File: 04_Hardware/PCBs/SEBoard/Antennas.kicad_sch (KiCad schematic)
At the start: 23 parts, among them J18 636101112001, J19 636101112001, J20 636101112001, J21 636101112001, U1 SC200EEMNA-E53-UGNDA

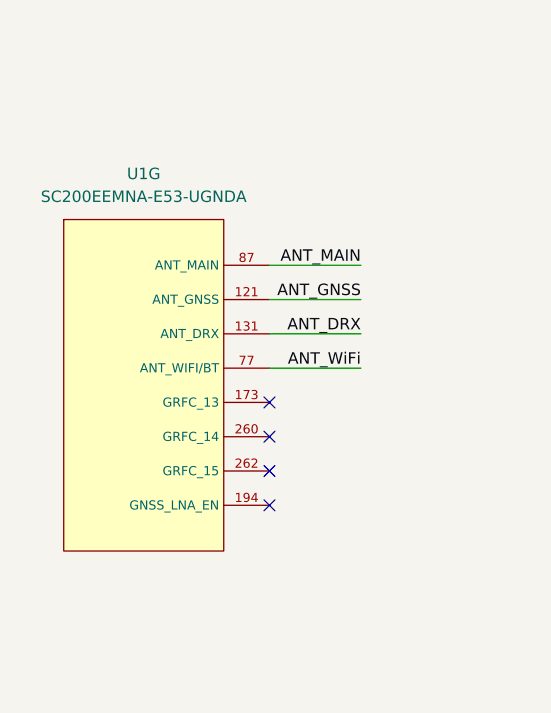
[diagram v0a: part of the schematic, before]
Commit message: feat(schematic): add SE250B4 symbol to schematic (unchecked)
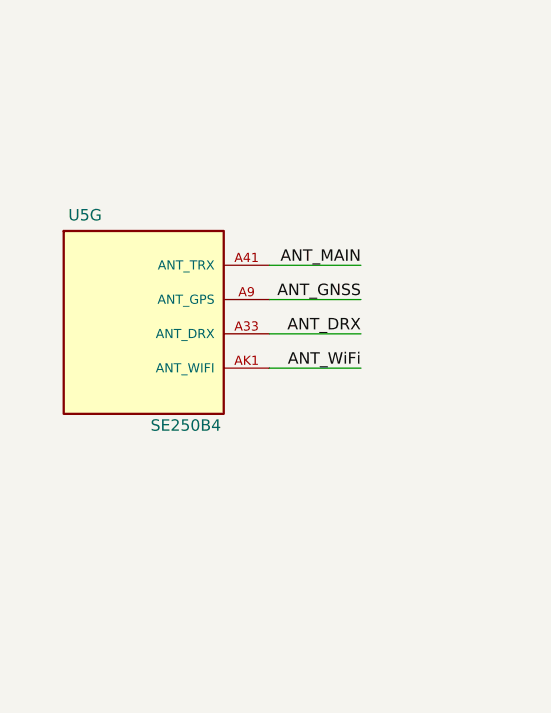
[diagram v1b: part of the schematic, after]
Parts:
- removed U1: SC200EEMNA-E53-UGNDA, SEBoard:SC200E_SC206E, symbol SEBoard:SC200E
- added U5: SE250B4, 000MCLib:XCVR_SE250B4-NA, symbol 000MCLib:SE250B4
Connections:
- net ANT_DRX: now also U5.A33 (ANT_DRX)
- net ANT_GNSS: now also U5.A9 (ANT_GPS)
- net ANT_MAIN: now also U5.A41 (ANT_TRX)
- net ANT_WiFi: now also U5.AK1 (ANT_WIFI)
- no-connect marks 4 -> 0

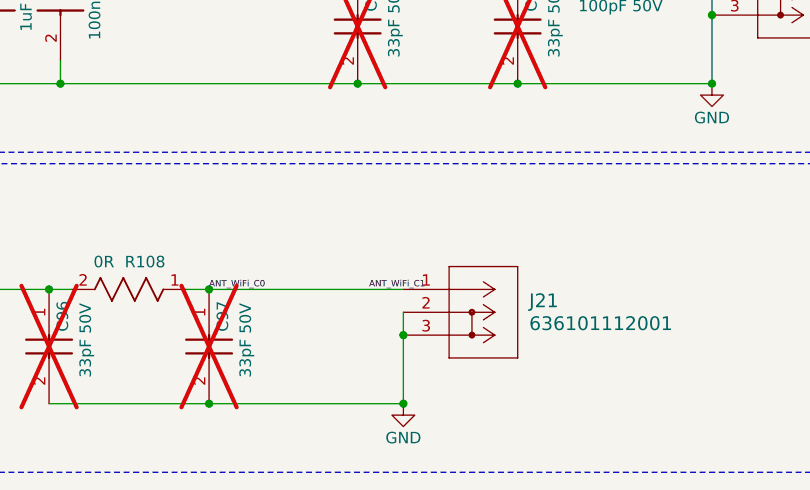
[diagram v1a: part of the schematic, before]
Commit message: feat: Updated schematic layout and moved new components to Layout
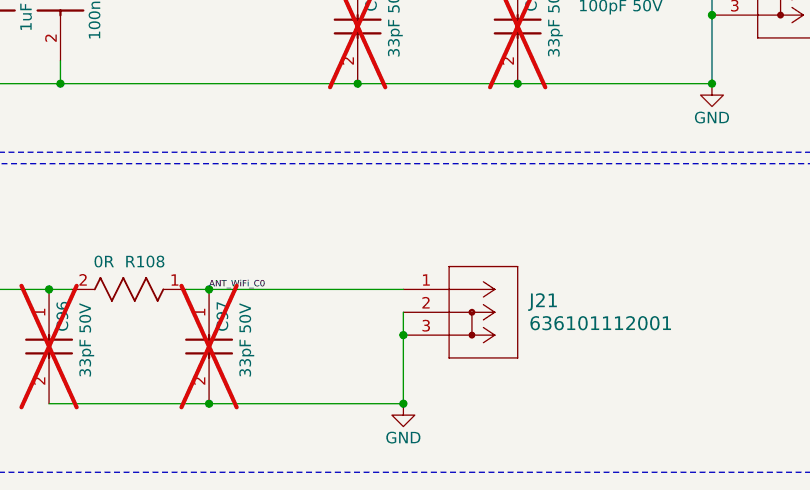
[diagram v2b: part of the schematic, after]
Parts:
- C51: footprint SEBoard:CAPC1005X55N -> 000MCLib:CAPC1005X55N; symbol SEBoard:GRM1555C1H101JA01J -> 000MCLib:GRM1555C1H101JA01J
- C53: footprint SEBoard:CAPC1005X55N -> 000MCLib:CAPC1005X55N; symbol SEBoard:GRM155R61H105KE05D -> 000MCLib:GRM155R61H105KE05D
- C55: footprint SEBoard:CAPC1005X55N -> 000MCLib:CAPC1005X55N; symbol SEBoard:GRM155R71A104KA01D -> 000MCLib:GRM155R71A104KA01D
- C90, C91, C92, C93, C94, C95, C96, C97: footprint SEBoard:CAPC1005X55N -> 000MCLib:CAPC1005X55N; symbol SEBoard:GRM1555C1H330JA01D -> 000MCLib:GRM1555C1H330JA01D
- J18, J19, J20, J21: footprint SEBoard:COAX2_636101112001_WRE -> 000MCLib:COAX2_636101112001_WRE; symbol SEBoard:636101112001 -> 000MCLib:636101112001
- L2: footprint SEBoard:INDC1005X60N -> 000MCLib:INDC1005X60N; symbol SEBoard:744784156A -> 000MCLib:744784156A
- R105, R106, R107, R108: footprint SEBoard:RC0402N_YAG -> 000MCLib:RC0402N_YAG; symbol SEBoard:RC0402JR-070RL -> 000MCLib:RC0402JR-070RL
- R16: footprint SEBoard:RC0402N_YAG -> 000MCLib:RC0402N_YAG; symbol SEBoard:RC0402JR-0710RL -> 000MCLib:RC0402JR-0710RL
- R69: footprint SEBoard:RESC2012X50N -> 000MCLib:RESC2012X50N; symbol SEBoard:CRCW08050000Z0EA -> 000MCLib:CRCW08050000Z0EA
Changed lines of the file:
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@@
 		)
 	)
-	(label "ANT_WiFi_C1"
-		(at 194.31 128.27 0)
-		(effects
-			(font
-				(size 0.7 0.7)
-			)
-			(justify left bottom)
-		)
-	)
 	(label "ANT_MAIN"
 		(at 72.39 82.55 180)
@@
 	)
 	(symbol
-		(lib_id "SEBoard:GRM155R61H105KE05D")
+		(lib_id "000MCLib:GRM155R61H105KE05D")
 		(at 152.4 96.52 270)
 		(unit 1)
@@
 			)
 		)
-		(property "Footprint" "SEBoard:CAPC1005X55N"
+		(property "Footprint" "000MCLib:CAPC1005X55N"
 			(at 56.21 105.41 0)
 			(effects
@@
 	)
 	(symbol
-		(lib_id "SEBoard:RC0402JR-0710RL")
+		(lib_id "000MCLib:RC0402JR-0710RL")
 		(at 204.47 83.82 0)
 		(unit 1)
@@
 			)
 		)
-		(property "Footprint" "SEBoard:RC0402N_YAG"
+		(property "Footprint" "000MCLib:RC0402N_YAG"
 			(at 198.12 83.82 0)
 			(effects
@@
 	)
 	(symbol
-		(lib_id "SEBoard:744784156A")
+		(lib_id "000MCLib:744784156A")
 		(at 218.44 83.82 0)
 		(unit 1)
@@
 			)
 		)
-		(property "Footprint" "SEBoard:INDC1005X60N"
+		(property "Footprint" "000MCLib:INDC1005X60N"
 			(at 234.95 180.01 0)
 			(effects
@@
 	)
 	(symbol
-		(lib_id "SEBoard:RC0402JR-070RL")
+		(lib_id "000MCLib:RC0402JR-070RL")
 		(at 167.64 128.27 0)
 		(unit 1)
@@
 			)
 		)
-		(property "Footprint" "SEBoard:RC0402N_YAG"
+		(property "Footprint" "000MCLib:RC0402N_YAG"
 			(at 161.29 128.27 0)
 			(effects
@@
 	)
 	(symbol
-		(lib_id "SEBoard:GRM1555C1H330JA01D")
+		(lib_id "000MCLib:GRM1555C1H330JA01D")
 		(at 210.82 99.06 270)
 		(unit 1)
@@
 			)
 		)
-		(property "Footprint" "SEBoard:CAPC1005X55N"
+		(property "Footprint" "000MCLib:CAPC1005X55N"
 			(at 114.63 107.95 0)
 			(effects
@@
 	)
 	(symbol
-		(lib_id "SEBoard:GRM1555C1H330JA01D")
+		(lib_id "000MCLib:GRM1555C1H330JA01D")
 		(at 205.74 59.69 270)
 		(unit 1)
@@
 			)
 		)
-		(property "Footprint" "SEBoard:CAPC1005X55N"
+		(property "Footprint" "000MCLib:CAPC1005X55N"
 			(at 109.55 68.58 0)
 			(effects
@@
 	)
 	(symbol
-		(lib_id "SEBoard:636101112001")
+		(lib_id "000MCLib:636101112001")
 		(at 241.3 95.25 0)
 		(unit 1)
@@
 			)
 		)
-		(property "Footprint" "SEBoard:COAX2_636101112001_WRE"
+		(property "Footprint" "000MCLib:COAX2_636101112001_WRE"
 			(at 240.284 90.17 0)
 			(effects
@@
 	)
 	(symbol
-		(lib_id "SEBoard:GRM155R71A104KA01D")
+		(lib_id "000MCLib:GRM155R71A104KA01D")
 		(at 160.02 96.52 270)
 		(unit 1)
@@
 			)
 		)
-		(property "Footprint" "SEBoard:CAPC1005X55N"
+		(property "Footprint" "000MCLib:CAPC1005X55N"
 			(at 63.83 105.41 0)
 			(effects
@@
 	)
 	(symbol
-		(lib_id "SEBoard:CRCW08050000Z0EA")
+		(lib_id "000MCLib:CRCW08050000Z0EA")
 		(at 121.92 96.52 180)
 		(unit 1)
@@
 			)
 		)
-		(property "Footprint" "SEBoard:RESC2012X50N"
+		(property "Footprint" "000MCLib:RESC2012X50N"
 			(at 107.95 0.33 0)
 			(effects
@@
 	)
 	(symbol
-		(lib_id "SEBoard:GRM1555C1H330JA01D")
+		(lib_id "000MCLib:GRM1555C1H330JA01D")
 		(at 223.52 59.69 270)
 		(unit 1)
@@
 			)
 		)
-		(property "Footprint" "SEBoard:CAPC1005X55N"
+		(property "Footprint" "000MCLib:CAPC1005X55N"
 			(at 127.33 68.58 0)
 			(effects
@@
 	)
 	(symbol
-		(lib_id "SEBoard:GRM1555C1H330JA01D")
+		(lib_id "000MCLib:GRM1555C1H330JA01D")
 		(at 137.16 59.69 270)
 		(unit 1)
@@
 			)
 		)
-		(property "Footprint" "SEBoard:CAPC1005X55N"
+		(property "Footprint" "000MCLib:CAPC1005X55N"
 			(at 40.97 68.58 0)
 			(effects
@@
 	)
 	(symbol
-		(lib_id "SEBoard:GRM1555C1H330JA01D")
+		(lib_id "000MCLib:GRM1555C1H330JA01D")
 		(at 176.53 134.62 270)
 		(unit 1)
@@
 			)
 		)
-		(property "Footprint" "SEBoard:CAPC1005X55N"
+		(property "Footprint" "000MCLib:CAPC1005X55N"
 			(at 80.34 143.51 0)
 			(effects
@@
 	)
 	(symbol
-		(lib_id "SEBoard:636101112001")
+		(lib_id "000MCLib:636101112001")
 		(at 207.01 130.81 0)
 		(unit 1)
@@
 			)
 		)
-		(property "Footprint" "SEBoard:COAX2_636101112001_WRE"
+		(property "Footprint" "000MCLib:COAX2_636101112001_WRE"
 			(at 205.994 125.73 0)
 			(effects
@@
 	)
 	(symbol
-		(lib_id "SEBoard:GRM1555C1H330JA01D")
+		(lib_id "000MCLib:GRM1555C1H330JA01D")
 		(at 193.04 99.06 270)
 		(unit 1)
@@
 			)
 		)
-		(property "Footprint" "SEBoard:CAPC1005X55N"
+		(property "Footprint" "000MCLib:CAPC1005X55N"
 			(at 96.85 107.95 0)
 			(effects
@@
 	)
 	(symbol
-		(lib_id "SEBoard:RC0402JR-070RL")
+		(lib_id "000MCLib:RC0402JR-070RL")
 		(at 201.93 92.71 0)
 		(unit 1)
@@
 			)
 		)
-		(property "Footprint" "SEBoard:RC0402N_YAG"
+		(property "Footprint" "000MCLib:RC0402N_YAG"
 			(at 195.58 92.71 0)
 			(effects
@@
 	)
 	(symbol
-		(lib_id "SEBoard:GRM1555C1H330JA01D")
+		(lib_id "000MCLib:GRM1555C1H330JA01D")
 		(at 158.75 134.62 270)
 		(unit 1)
@@
 			)
 		)
-		(property "Footprint" "SEBoard:CAPC1005X55N"
+		(property "Footprint" "000MCLib:CAPC1005X55N"
 			(at 62.56 143.51 0)
 			(effects
@@
 	)
 	(symbol
-		(lib_id "SEBoard:RC0402JR-070RL")
+		(lib_id "000MCLib:RC0402JR-070RL")
 		(at 214.63 53.34 0)
 		(unit 1)
@@
 			)
 		)
-		(property "Footprint" "SEBoard:RC0402N_YAG"
+		(property "Footprint" "000MCLib:RC0402N_YAG"
 			(at 208.28 53.34 0)
 			(effects
@@
 	)
 	(symbol
-		(lib_id "SEBoard:636101112001")
+		(lib_id "000MCLib:636101112001")
 		(at 242.57 55.88 0)
 		(unit 1)
@@
 			)
 		)
-		(property "Footprint" "SEBoard:COAX2_636101112001_WRE"
+		(property "Footprint" "000MCLib:COAX2_636101112001_WRE"
 			(at 241.554 50.8 0)
 			(effects
@@
 	)
 	(symbol
-		(lib_id "SEBoard:GRM1555C1H330JA01D")
+		(lib_id "000MCLib:GRM1555C1H330JA01D")
 		(at 119.38 59.69 270)
 		(unit 1)
@@
 			)
 		)
-		(property "Footprint" "SEBoard:CAPC1005X55N"
+		(property "Footprint" "000MCLib:CAPC1005X55N"
 			(at 23.19 68.58 0)
 			(effects
@@
 	)
 	(symbol
-		(lib_id "SEBoard:636101112001")
+		(lib_id "000MCLib:636101112001")
 		(at 156.21 55.88 0)
 		(unit 1)
@@
 			)
 		)
-		(property "Footprint" "SEBoard:COAX2_636101112001_WRE"
+		(property "Footprint" "000MCLib:COAX2_636101112001_WRE"
 			(at 155.194 50.8 0)
 			(effects
@@
 	)
 	(symbol
-		(lib_id "SEBoard:GRM1555C1H101JA01J")
+		(lib_id "000MCLib:GRM1555C1H101JA01J")
 		(at 222.25 92.71 0)
 		(unit 1)
@@
 			)
 		)
-		(property "Footprint" "SEBoard:CAPC1005X55N"
+		(property "Footprint" "000MCLib:CAPC1005X55N"
 			(at 231.14 188.9 0)
 			(effects
@@
 	)
 	(symbol
-		(lib_id "SEBoard:RC0402JR-070RL")
+		(lib_id "000MCLib:RC0402JR-070RL")
 		(at 128.27 53.34 0)
 		(unit 1)
@@
 			)
 		)
-		(property "Footprint" "SEBoard:RC0402N_YAG"
+		(property "Footprint" "000MCLib:RC0402N_YAG"
 			(at 121.92 53.34 0)
 			(effects
